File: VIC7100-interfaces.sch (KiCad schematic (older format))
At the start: 59 parts, among them Q5 DMG1012UW, U13 VIC7100

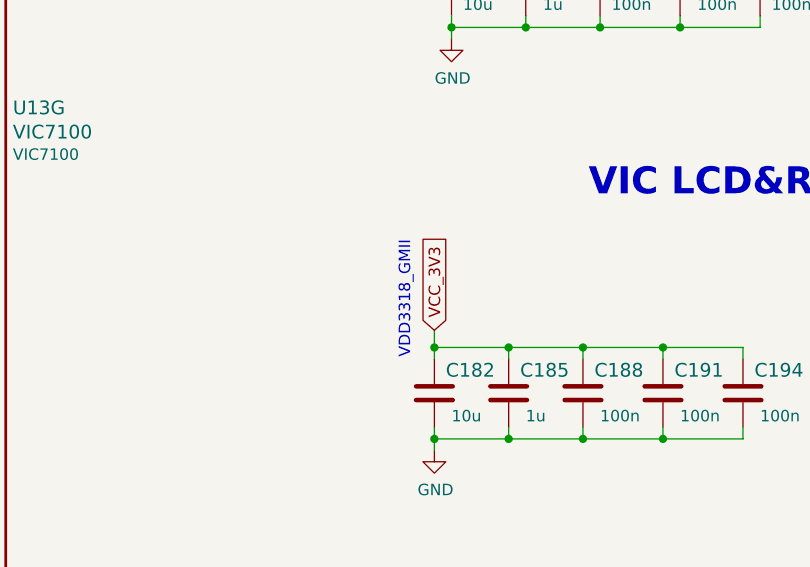
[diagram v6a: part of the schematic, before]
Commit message: Updated component placement - VIC interfaces decoupling done
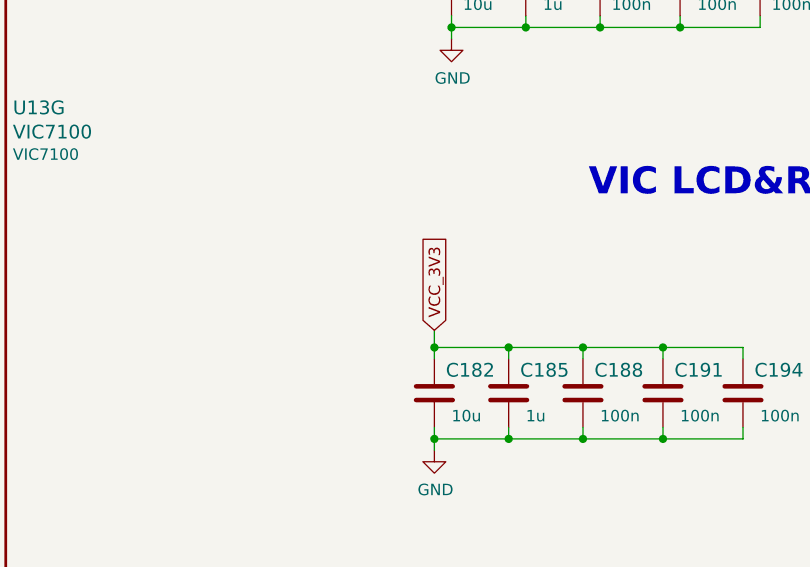
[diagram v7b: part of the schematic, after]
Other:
- note removed: "VDD3318_GMII"
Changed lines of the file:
@@
 	1    0    0    -1
 $EndComp
-Text GLabel 5325 10175 1    50   Input ~ 0
-VCC_3V3
 NoConn ~ 5650 8600
 NoConn ~ 5650 8700
@@
 	5700 4100 5475 4100
 Connection ~ 5700 4100
-Text GLabel 5475 4100 0    50   Input ~ 0
-VCC_3V3
 Wire Wire Line
 	5700 1300 5275 1300
@@
 Wire Wire Line
 	5625 7775 5400 7775
-Text GLabel 5400 7775 0    50   Input ~ 0
-VCC_3V3
 Wire Wire Line
 	5625 7775 5625 7875
@@
 Text GLabel 5025 5275 0    50   Input ~ 0
 RGMII_TXEN
-Text GLabel 8700 1350 0    50   Input ~ 0
-VCC_0V9
 Wire Wire Line
 	8700 1350 8975 1350
-Text GLabel 8700 1650 0    50   Input ~ 0
-VCC_1V8
 Wire Wire Line
 	8700 1650 8975 1650
@@
 Wire Wire Line
 	12850 4800 13200 4800
-Text Notes 11750 4450 1    50   ~ 0
-VDD3318_GMII
 Text GLabel 13625 4325 1    50   Input ~ 0
 VCC_3V3
@@
 Wire Wire Line
 	4725 1500 4925 1500
+Text GLabel 5325 10175 1    50   Input ~ 0
+VCC_3V3
+Text GLabel 5400 7775 0    50   Input ~ 0
+VCC_3V3
+Text GLabel 5475 4100 0    50   Input ~ 0
+VCC_3V3
+Text GLabel 8700 1650 0    50   Input ~ 0
+VCC_1V8
+Text GLabel 8700 1350 0    50   Input ~ 0
+VCC_0V9
 $EndSCHEMATC

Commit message: Finished component placement
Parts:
- removed R122: R_10k_0402, arvsom-footprints:0402-res, symbol arvsom:R_10k_0402
- removed R55, R56, R57, R59: R_33R_0402, arvsom-footprints:0402-res, symbol arvsom:R_33R_0402
- added R122: R_10k_0201, arvsom-footprints:0201-res, symbol arvsom:R_10k_0201
- added R20: 4x33R_0201_array, arvsom-footprints:EXB18V, symbol arvsom:4x33R_0201_array
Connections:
- net labels added: HDMI_I2S_TX0
- net labels removed: HDMI_I2STX0
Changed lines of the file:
@@
 Text GLabel 2125 7475 0    50   Input ~ 0
 I2C0_SCL
-Text GLabel 1325 4075 0    50   Input ~ 0
-HDMI_I2STX0
-Text GLabel 1325 3975 0    50   Input ~ 0
+Text GLabel 1275 3975 0    50   Input ~ 0
 HDMI_LRCLK
-Text GLabel 1325 3775 0    50   Input ~ 0
+Text GLabel 1275 3775 0    50   Input ~ 0
 HDMI_12MHZ
 Text GLabel 1325 4475 0    50   Input ~ 0
 HDMI_INT
-Text GLabel 1325 3875 0    50   Input ~ 0
+Text GLabel 1275 3875 0    50   Input ~ 0
 HDMI_BCLK
 NoConn ~ 2125 7675
@@
 NoConn ~ 2125 8175
 $Comp
-L arvsom:R_33R_0402 R55
-U 1 1 619E8438
-P 1600 4075
-F 0 "R55" H 1400 4025 60  0000 C CNN
-F 1 "R_33R_0402" H 1600 3925 60  0001 C CNN
-F 2 "arvsom-footprints:0402-res" H 1800 4275 60  0001 L CNN
-F 3 "" H 1600 4075 50  0001 C CNN
-F 4 "Vishay" H 1800 4475 60  0001 L CNN "Manufacturer"
-F 5 "CRCW040233R0FKED" H 1800 4375 60  0001 L CNN "MPN"
-F 6 "33R" H 1800 4025 50  0000 C CNN "Val"
-	1    1600 4075
-	1    0    0    -1
-$EndComp
-$Comp
-L arvsom:R_33R_0402 R56
-U 1 1 619EF7E3
-P 1600 3975
-F 0 "R56" H 1400 3925 60  0000 C CNN
-F 1 "R_33R_0402" H 1600 3825 60  0001 C CNN
-F 2 "arvsom-footprints:0402-res" H 1800 4175 60  0001 L CNN
-F 3 "" H 1600 3975 50  0001 C CNN
-F 4 "Vishay" H 1800 4375 60  0001 L CNN "Manufacturer"
-F 5 "CRCW040233R0FKED" H 1800 4275 60  0001 L CNN "MPN"
-F 6 "33R" H 1800 3925 50  0000 C CNN "Val"
-	1    1600 3975
-	1    0    0    -1
-$EndComp
-$Comp
-L arvsom:R_33R_0402 R57
-U 1 1 619F3AD5
-P 1600 3775
-F 0 "R57" H 1400 3725 60  0000 C CNN
-F 1 "R_33R_0402" H 1600 3625 60  0001 C CNN
-F 2 "arvsom-footprints:0402-res" H 1800 3975 60  0001 L CNN
-F 3 "" H 1600 3775 50  0001 C CNN
-F 4 "Vishay" H 1800 4175 60  0001 L CNN "Manufacturer"
-F 5 "CRCW040233R0FKED" H 1800 4075 60  0001 L CNN "MPN"
-F 6 "33R" H 1800 3725 50  0000 C CNN "Val"
-	1    1600 3775
-	1    0    0    -1
-$EndComp
-$Comp
 L arvsom:R_33R_0402 R58
 U 1 1 619F4460
@@
 	1    0    0    -1
 $EndComp
-$Comp
-L arvsom:R_33R_0402 R59
-U 1 1 619F4C47
-P 1600 3875
-F 0 "R59" H 1400 3825 60  0000 C CNN
-F 1 "R_33R_0402" H 1600 3725 60  0001 C CNN
-F 2 "arvsom-footprints:0402-res" H 1800 4075 60  0001 L CNN
-F 3 "" H 1600 3875 50  0001 C CNN
-F 4 "Vishay" H 1800 4275 60  0001 L CNN "Manufacturer"
-F 5 "CRCW040233R0FKED" H 1800 4175 60  0001 L CNN "MPN"
-F 6 "33R" H 1800 3825 50  0000 C CNN "Val"
-	1    1600 3875
-	1    0    0    -1
-$EndComp
 Wire Wire Line
-	1325 4075 1450 4075
+	1275 4075 1400 4075
 Wire Wire Line
 	1750 4075 2125 4075
 Wire Wire Line
-	1325 3975 1450 3975
+	1275 3975 1400 3975
 Wire Wire Line
-	1325 3775 1450 3775
+	1275 3775 1400 3775
 Wire Wire Line
 	1325 4475 1450 4475
 Wire Wire Line
-	1325 3875 1450 3875
+	1275 3875 1400 3875
 Wire Wire Line
 	1750 3975 2125 3975
@@
 Text GLabel 2325 9025 2    50   Input ~ 0
 VCC_3V3
-$Comp
-L arvsom:R_10k_0402 R122
-U 1 1 611FAF4E
-P 2025 9975
-F 0 "R122" H 1925 9875 60  0000 C CNN
-F 1 "R_10k_0402" H 2025 9825 60  0001 C CNN
-F 2 "arvsom-footprints:0402-res" H 2225 10175 60  0001 L CNN
-F 3 "" H 2025 9975 50  0001 C CNN
-F 4 "VISHAY" H 2225 10375 60  0001 L CNN "Manufacturer"
-F 5 "CRCW040210K0FKEDHP" H 2225 10275 60  0001 L CNN "MPN"
-F 6 "10k" H 2175 9875 50  0000 C CNN "Val"
-F 7 "DNP" H 1825 10025 50  0000 C CNN "Populate"
-	1    2025 9975
-	1    0    0    -1
-$EndComp
 Wire Wire Line
 	2175 9975 2325 9975
@@
 Text GLabel 8700 1350 0    50   Input ~ 0
 VCC_0V9
+$Comp
+L arvsom:R_10k_0201 R122
+U 1 1 61BBAC32
+P 2025 9975
+F 0 "R122" H 1775 10025 60  0000 C CNN
+F 1 "R_10k_0201" H 2025 9825 60  0001 C CNN
+F 2 "arvsom-footprints:0201-res" H 2225 10175 60  0001 L CNN
+F 3 "" H 2025 9975 50  0001 C CNN
+F 4 "YAGEO" H 2225 10375 60  0001 L CNN "Manufacturer"
+F 5 "RC0201FR-0710KL" H 2225 10275 60  0001 L CNN "MPN"
+F 6 "10k" H 2250 10025 50  0000 C CNN "Val"
+F 7 "DNP" H 2025 9975 50  0000 C CNN "Populate"
+	1    2025 9975
+	1    0    0    -1
+$EndComp
+$Comp
+L arvsom:4x33R_0201_array R20
+U 1 1 61C5432D
+P 1600 4175
+F 0 "R20" H 1850 4325 60  0000 C CNN
+F 1 "4x33R_0201_array" H 1575 4756 60  0001 C CNN
+F 2 "arvsom-footprints:EXB18V" H 1400 4925 60  0001 L CNN
+F 3 "http://industrial.panasonic.com/cdbs/www-data/pdf/AOC0000/AOC0000C14.pdf" H 1400 4925 60  0001 L CNN
+F 4 "EXB-18V330JX" H 1400 5125 60  0001 L CNN "MPN"
+F 5 "Panasonic" H 1400 5025 60  0001 L CNN "Manufacturer"
+	1    1600 4175
+	1    0    0    -1
+$EndComp
+Text GLabel 1275 4075 0    50   Input ~ 0
+HDMI_I2S_TX0
 $EndSCHEMATC
